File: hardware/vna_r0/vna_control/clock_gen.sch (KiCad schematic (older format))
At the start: 1 part

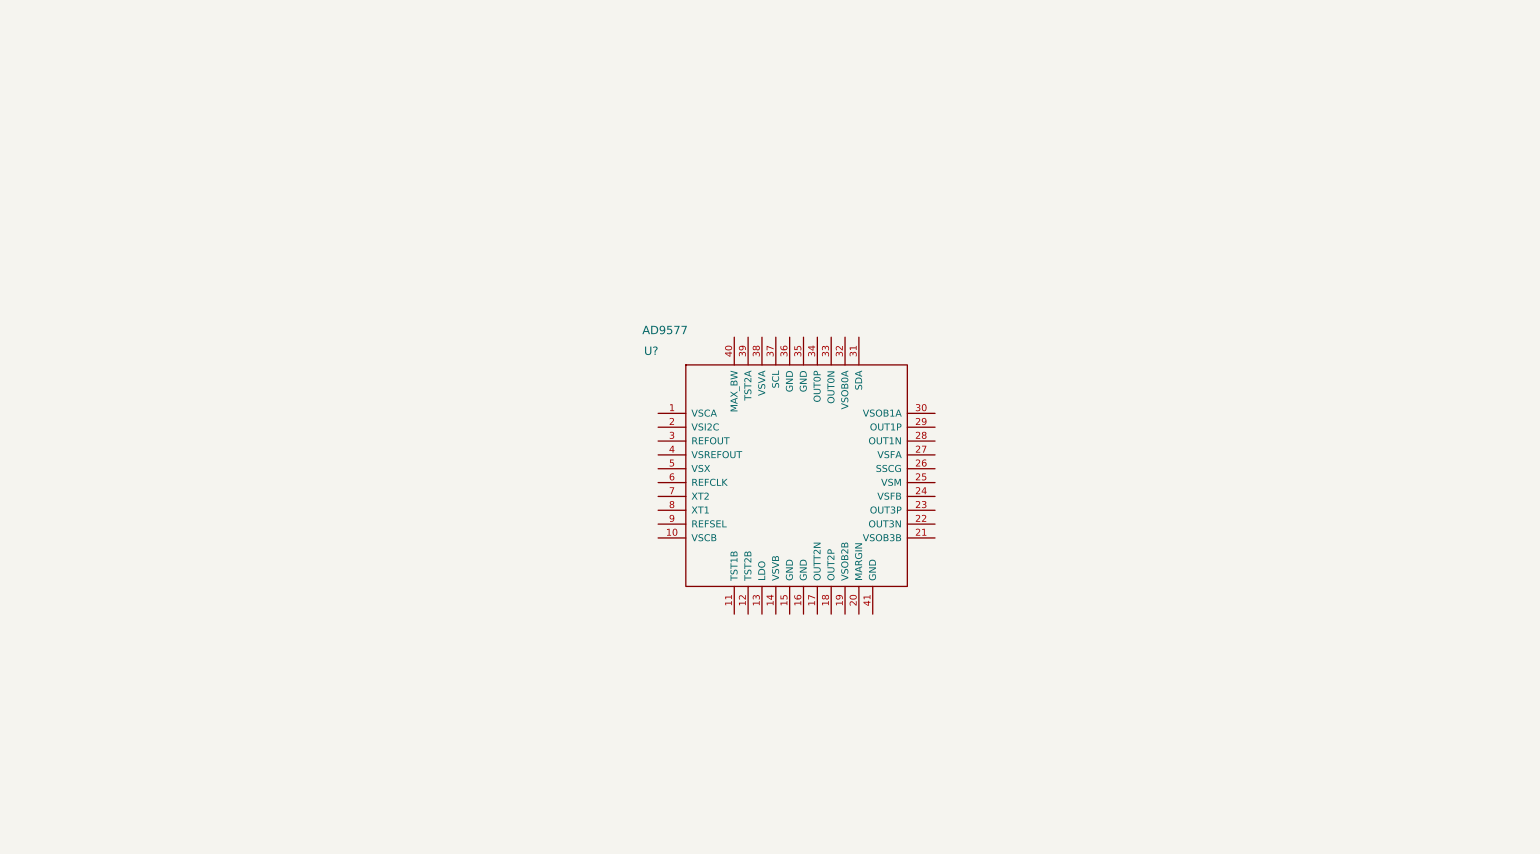
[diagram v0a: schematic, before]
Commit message: started on vna r0 beaglebone cape
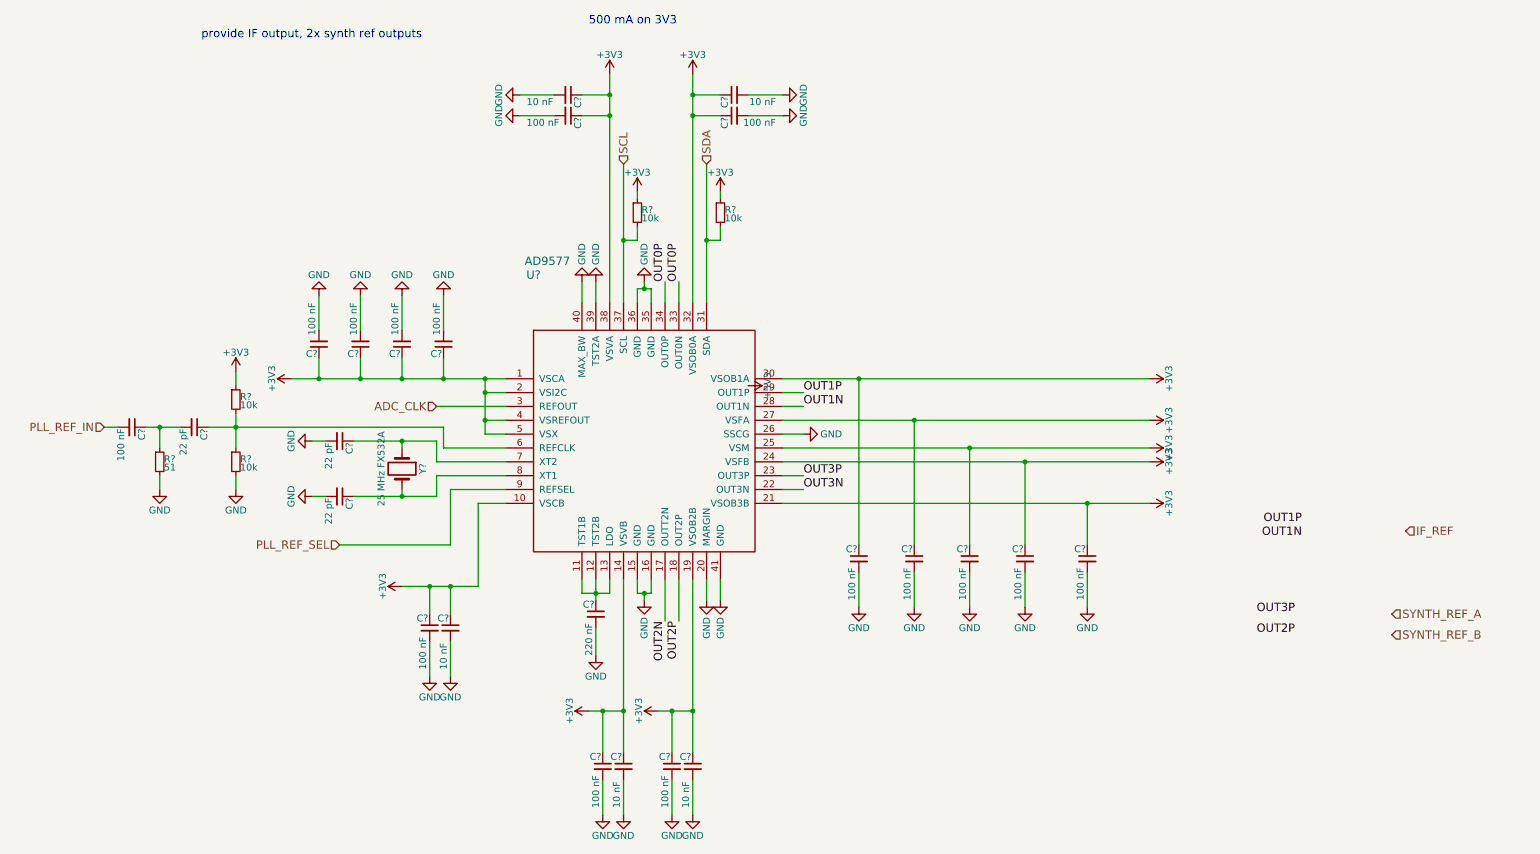
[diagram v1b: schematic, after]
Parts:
- removed U?: AD9577, symbol AD9577
- added C? (x3): 22 pF, symbol C_Small
- added C? (x15): 100 nF, symbol C_Small
- added C? (x5): 10 nF, symbol C_Small
- added C?: 220 nF, symbol C_Small
- added R? (x4): 10k, symbol R_Small
- added R?: 51, symbol R_Small
- added U?: AD9577, symbol AD9577
- added Y?: 25 MHz FX532A, symbol Crystal
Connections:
- new net: C?.1, U?.11 (TST1B), U?.12 (TST2B), U?.13 (LDO)
- new net: C?.1, R?.1, R?.2, U?.6 (REFCLK)
- new net: C?.1, U?.7 (XT2), Y?.1
- new net: C?.1, U?.8 (XT1), Y?.2
- new net: C?.1, C?.2, R?.1
- new net +3V3: C?.1, C?.1, C?.1, C?.1, C?.1, C?.1, C?.1, C?.1, C?.1, C?.1, C?.1, C?.1, C?.1, C?.1, C?.1, C?.1, C?.1, C?.1, C?.1, R?.1, R?.1, R?.1, U?.1 (VSCA), U?.10 (VSCB), U?.14 (VSVB), U?.19 (VSOB2B), U?.2 (VSI2C), U?.21 (VSOB3B), U?.24 (VSFB), U?.25 (VSM), U?.27 (VSFA), U?.30 (VSOB1A), U?.32 (VSOB0A), U?.38 (VSVA), U?.4 (VSREFOUT), U?.5 (VSX)
- new net ADC_CLK: U?.3 (REFOUT)
- new net GND: C?.2, C?.2, C?.2, C?.2, C?.2, C?.2, C?.2, C?.2, C?.2, C?.2, C?.2, C?.2, C?.2, C?.2, C?.2, C?.2, C?.2, C?.2, C?.2, C?.2, C?.2, C?.2, R?.2, R?.2, U?.15 (GND), U?.16 (GND), U?.20 (MARGIN), U?.26 (SSCG), U?.35 (GND), U?.36 (GND), U?.39 (TST2A), U?.40 (MAX_BW), U?.41 (GND)
- new net OUT0P: U?.33 (OUT0N), U?.34 (OUT0P)
- new net OUT1N: U?.28 (OUT1N)
- new net OUT1P: U?.29 (OUT1P)
- new net OUT2N: U?.17 (OUTT2N)
- new net OUT2P: U?.18 (OUT2P)
- new net OUT3N: U?.22 (OUT3N)
- new net OUT3P: U?.23 (OUT3P)
- new net PLL_REF_IN: C?.2
- new net PLL_REF_SEL: U?.9 (REFSEL)
- new net SCL: R?.2, U?.37 (SCL)
- new net SDA: R?.2, U?.31 (SDA)
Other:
- note added: "500 mA on 3V3"
- note added: "provide IF output, 2x synth ref outputs"

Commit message: started layout of vna r0 control cape
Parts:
- added C225, C226, C227: 100 nF, Capacitors_SMD:C_0402, symbol C_Small
- added L201: L_Small, Resistors_SMD:R_0805, symbol L_Small
- added R206, R207, R208, R209, R210, R211, R216, R217, R218: 10k, Resistors_SMD:R_0402, symbol R_Small
- added R212, R213, R214, R215: DNP, Resistors_SMD:R_0402, symbol R_Small
- added U202: CONN_SMA_2GND, vna_footprints:734120110_ufl_umc, symbol CONN_SMA_2GND
- C201, C202, C203, C204, C205, C206, C207, C208, C209, C210, C211, C212, C213, C214, C215, C216, C217, C218, C219, C220, C221, C222, C223, C224: renamed from C?; footprint (none) -> Capacitors_SMD:C_0402
- R201, R202, R203, R204, R205: renamed from R?; footprint (none) -> Resistors_SMD:R_0402
- U201: renamed from U?; footprint (none) -> Housings_DFN_QFN:QFN-40-1EP_6x6mm_Pitch0.5mm
- Y201: renamed from Y?; value 25 MHz FX532A -> 26 MHz FX532A; footprint (none) -> Crystals:ABM3
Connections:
- net OUT2N is gone; now on net SYNTH_REF_B: U201.17 (OUTT2N)
- net OUT2P is gone; now on net SYNTH_REF_A: U201.18 (OUT2P)
- net +3V3: now also R212.1, R214.1, R216.1
- net GND: now also C225.2, C226.2, R206.1, R208.2, R209.1, R211.2, R213.2, R215.2, R217.2, R218.2, U202.2 (GND), U202.3 (GND)
- net IF_REF: now also C227.1
- net OUT0P: now also R206.2, R207.1; no longer U201.33 (OUT0N)
- net OUT1N: now also C225.1, L201.1, R216.2, R217.1
- net OUT1P: now also R218.1, U202.1 (RF)
- net OUT3N: now also R210.2, R211.1
- net OUT3P: now also R209.2, R210.1
- net SYNTH_REF_A: now also R214.2, R215.1
- net SYNTH_REF_B: now also R212.2, R213.1
- new net: C226.1, C227.2, L201.2
- new net OUT0N: R207.2, R208.1, U201.33 (OUT0N)

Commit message: finished vna control cape
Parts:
- removed Y201: 26 MHz FX532A, Crystals:ABM3, symbol Crystal
- added Y201: 26 MHz 7M-26.000MEEQ-T, vna_footprints:crystal_FA238-TSX3225, symbol Crystal_GND24
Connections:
- net GND: now also Y201.2, Y201.4
- net at C204.1, U201.7 (XT2): now also Y201.1
- net at C205.1, U201.8 (XT1): now also Y201.3
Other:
- note removed: "provide IF output, 2x synth ref outputs"

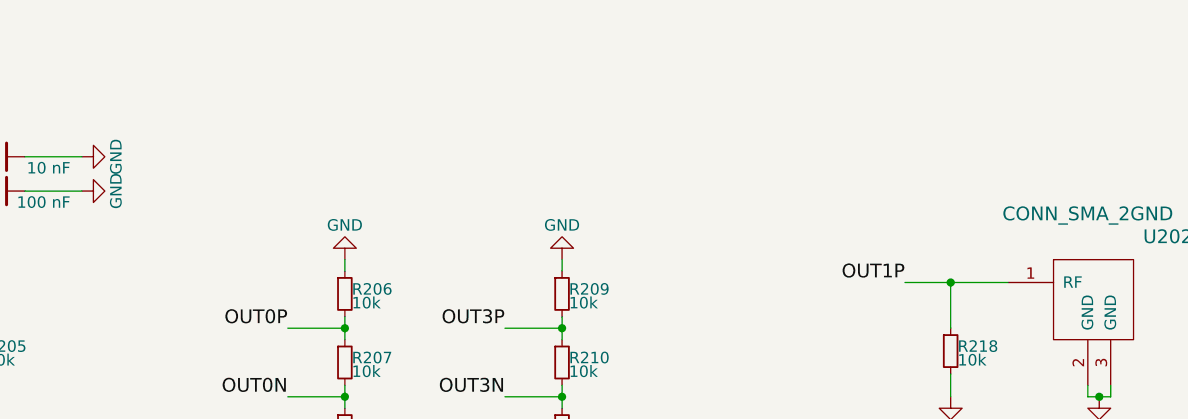
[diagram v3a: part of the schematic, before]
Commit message: started porting sofware to next revision synth, wrote ad9577 driver
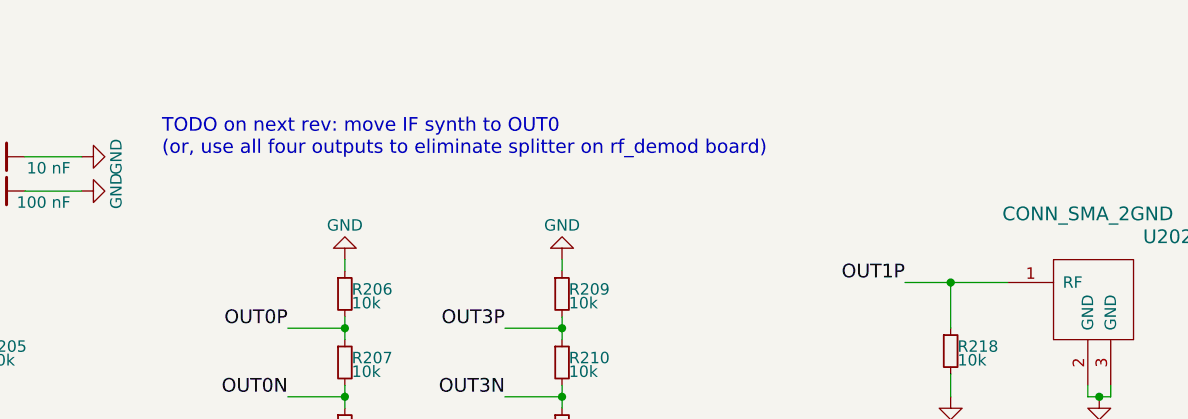
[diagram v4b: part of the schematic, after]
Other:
- note added: "TODO on next rev: move IF synth to OUT0\n(or, use all four outputs to eliminate splitter on rf_demod board)"
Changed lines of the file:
@@
 Wire Wire Line
 	3550 4200 3950 4200
+Text Notes 6300 1550 0    60   ~ 0
+TODO on next rev: move IF synth to OUT0\n(or, use all four outputs to eliminate splitter on rf_demod board)
 $EndSCHEMATC

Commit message: add if filter component values to vna_control, fix port control line swap on vna_rf board, switch TPS2041B amp 5v switch ~enable to pullup
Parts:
- C225: value 100 nF -> 18 pF
- C226: value 100 nF -> 120 pF
- L201: value L_Small -> 130 nH
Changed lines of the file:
@@
 P 10000 3600
 F 0 "C225" H 10010 3670 50  0000 L CNN
-F 1 "100 nF" V 10050 3300 50  0000 L CNN
+F 1 "18 pF" V 10050 3300 50  0000 L CNN
 F 2 "Capacitors_SMD:C_0402" H 10000 3600 50  0001 C CNN
 F 3 "" H 10000 3600 50  0001 C CNN
@@
 P 10400 3600
 F 0 "C226" H 10410 3670 50  0000 L CNN
-F 1 "100 nF" V 10450 3300 50  0000 L CNN
+F 1 "120 pF" V 10450 3300 50  0000 L CNN
 F 2 "Capacitors_SMD:C_0402" H 10400 3600 50  0001 C CNN
 F 3 "" H 10400 3600 50  0001 C CNN
@@
 P 10200 3450
 F 0 "L201" H 10230 3490 50  0000 L CNN
-F 1 "L_Small" H 10230 3410 50  0000 L CNN
+F 1 "130 nH" H 10230 3410 50  0000 L CNN
 F 2 "Resistors_SMD:R_0805" H 10200 3450 50  0001 C CNN
 F 3 "" H 10200 3450 50  0001 C CNN
